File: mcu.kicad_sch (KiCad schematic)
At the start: 2 parts

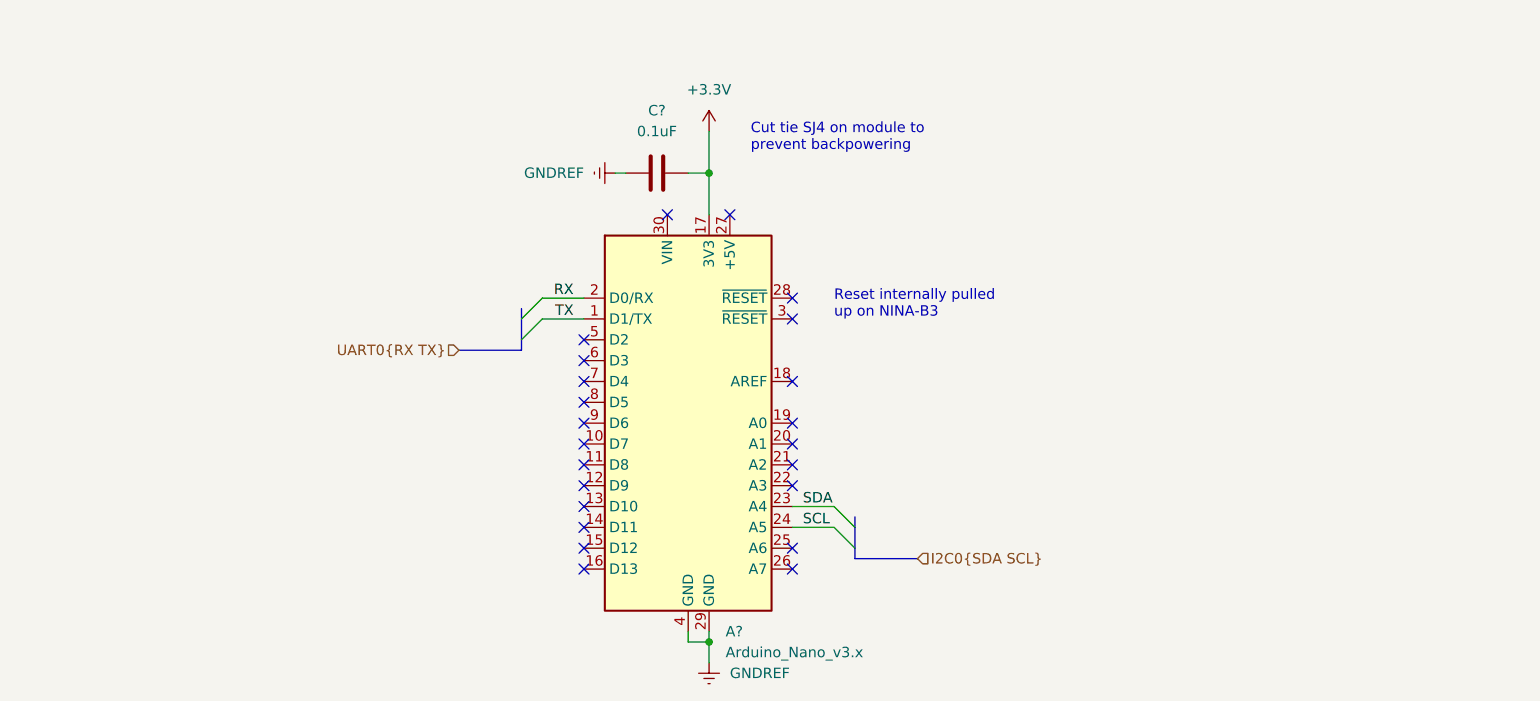
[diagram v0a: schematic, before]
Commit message: create IO busses
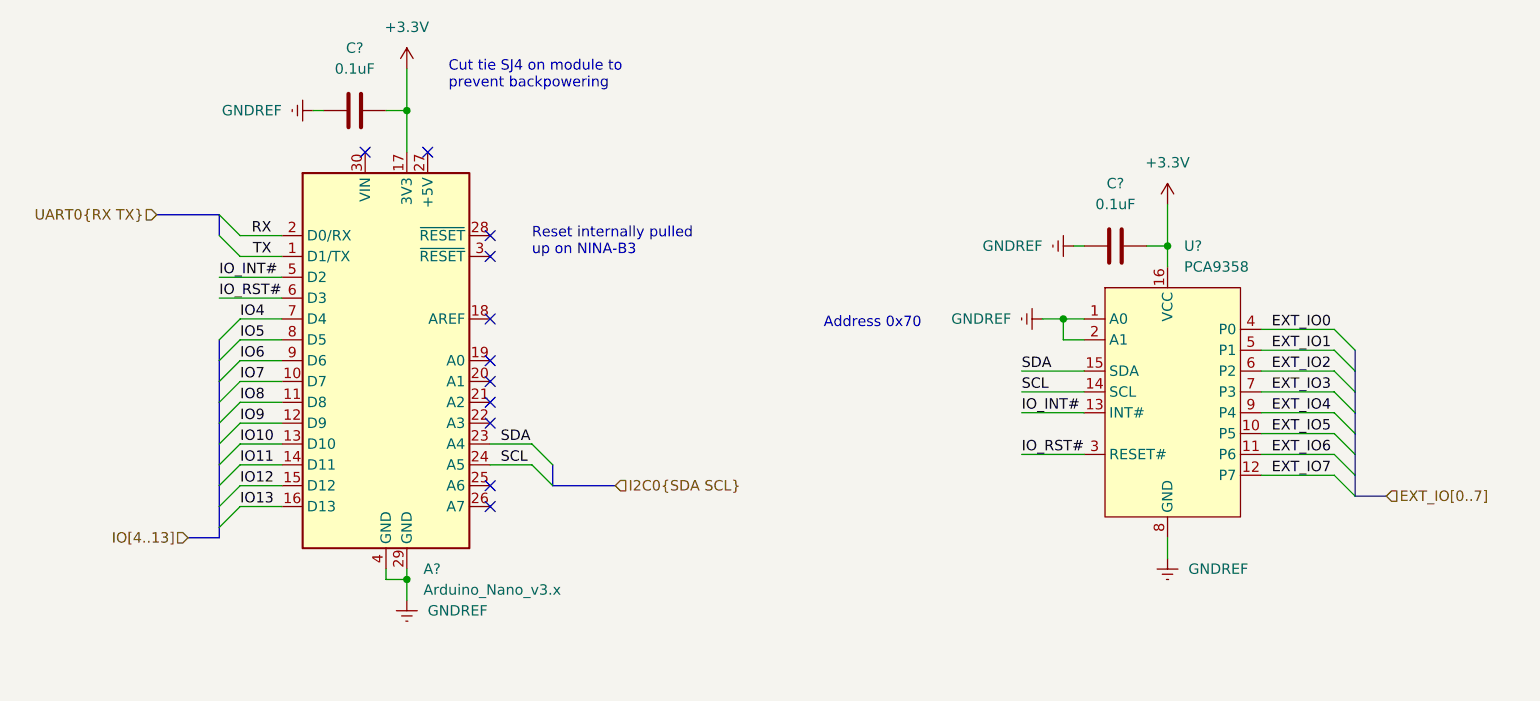
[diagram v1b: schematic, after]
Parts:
- added C?: 0.1uF, Capacitor_SMD:C_0805_2012Metric_Pad1.18x1.45mm_HandSolder, symbol Device:C
- added U?: PCA9358, Package_SO:SOIC-16W_7.5x10.3mm_P1.27mm, symbol Toadly:PCA9358
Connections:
- net +3.3V: now also C?.1, U?.16 (VCC)
- net GNDREF: now also C?.2, U?.1 (A0), U?.2 (A1), U?.8 (GND)
- net SCL: now also U?.14 (SCL)
- net SDA: now also U?.15 (SDA)
- net IO7: now reaches A?.10 (D7)
- net IO8: now reaches A?.11 (D8)
- net IO9: now reaches A?.12 (D9)
- net IO10: now reaches A?.13 (D10)
- net IO11: now reaches A?.14 (D11)
- net IO12: now reaches A?.15 (D12)
- net IO13: now reaches A?.16 (D13)
- net IO_INT#: now reaches A?.5 (D2)
- net IO_INT#: now also U?.13 (INT#)
- net IO_RST#: now reaches A?.6 (D3)
- net IO_RST#: now also U?.3 (RESET#)
- net IO4: now reaches A?.7 (D4)
- net IO5: now reaches A?.8 (D5)
- net IO6: now reaches A?.9 (D6)
- new net EXT_IO0: U?.4 (P0)
- new net EXT_IO1: U?.5 (P1)
- new net EXT_IO2: U?.6 (P2)
- new net EXT_IO3: U?.7 (P3)
- new net EXT_IO4: U?.9 (P4)
- new net EXT_IO5: U?.10 (P5)
- new net EXT_IO6: U?.11 (P6)
- new net EXT_IO7: U?.12 (P7)
- no-connect marks 23 -> 11
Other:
- note added: "Address 0x70"
- moved on the sheet: A?, C?

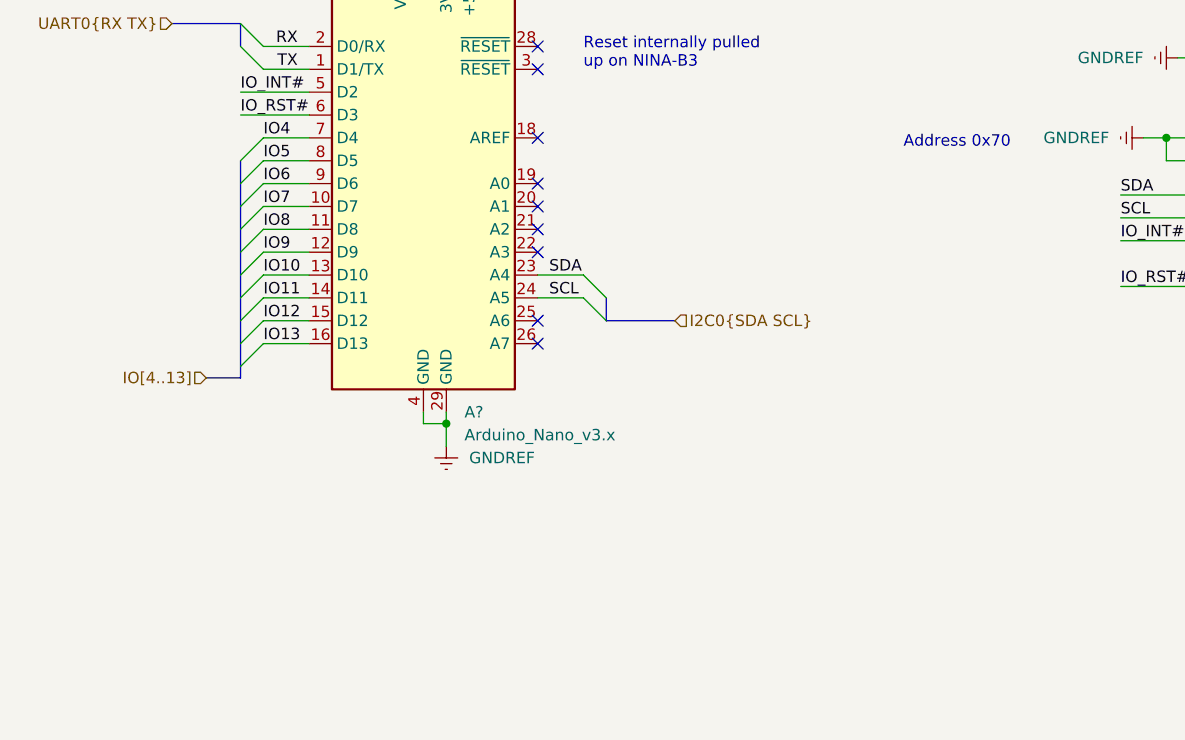
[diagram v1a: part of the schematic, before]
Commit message: add analog pins to IO and I2C pullup slots
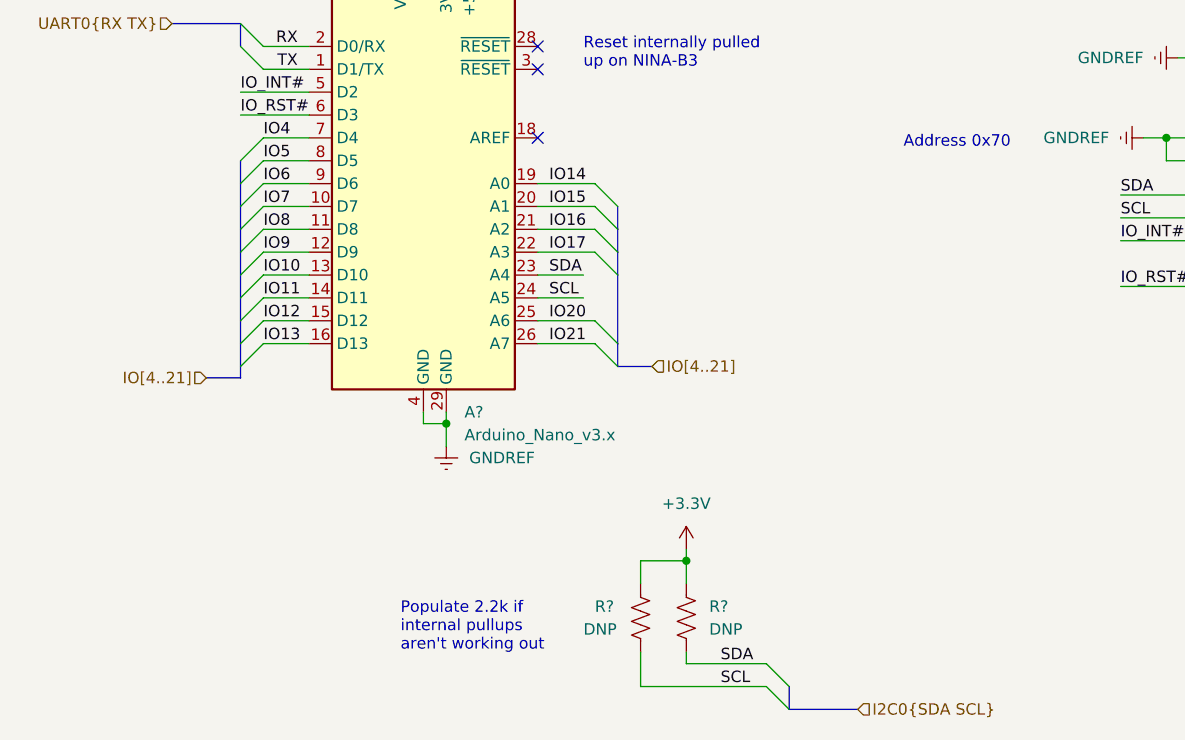
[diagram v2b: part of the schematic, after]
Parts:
- added R? (x2): DNP, Resistor_SMD:R_0805_2012Metric_Pad1.20x1.40mm_HandSolder, symbol Device:R_US
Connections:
- net +3.3V: now also R?.1, R?.2
- net SCL: now also R?.1
- net SDA: now also R?.2
- net IO14: now reaches A?.19 (A0)
- net IO15: now reaches A?.20 (A1)
- net IO16: now reaches A?.21 (A2)
- net IO17: now reaches A?.22 (A3)
- net IO20: now reaches A?.25 (A6)
- net IO21: now reaches A?.26 (A7)
- no-connect marks 11 -> 5
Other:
- note added: "Populate 2.2k if internal pullups aren't working out"

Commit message: annotate schematic
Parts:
- gave numbers to parts that had none: 6
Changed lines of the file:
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@@
   (symbol (lib_id "Device:C") (at 191.77 66.04 270) (mirror x) (unit 1)
     (in_bom yes) (on_board yes) (fields_autoplaced)
-    (property "Reference" "C?" (id 0) (at 191.77 58.42 90))
+    (property "Reference" "C6" (id 0) (at 191.77 58.42 90))
     (property "Value" "0.1uF" (id 1) (at 191.77 60.96 90))
     (property "Footprint" "Capacitor_SMD:C_0805_2012Metric_Pad1.18x1.45mm_HandSolder" (id 2) (at 187.96 65.0748 0)
@@
   (symbol (lib_id "Device:C") (at 99.06 49.53 270) (mirror x) (unit 1)
     (in_bom yes) (on_board yes) (fields_autoplaced)
-    (property "Reference" "C?" (id 0) (at 99.06 41.91 90))
+    (property "Reference" "C5" (id 0) (at 99.06 41.91 90))
     (property "Value" "0.1uF" (id 1) (at 99.06 44.45 90))
     (property "Footprint" "Capacitor_SMD:C_0805_2012Metric_Pad1.18x1.45mm_HandSolder" (id 2) (at 95.25 48.5648 0)
@@
   (symbol (lib_id "power:GNDREF") (at 93.98 49.53 270) (mirror x) (unit 1)
     (in_bom yes) (on_board yes) (fields_autoplaced)
-    (property "Reference" "#PWR?" (id 0) (at 87.63 49.53 0)
+    (property "Reference" "#PWR017" (id 0) (at 87.63 49.53 0)
       (effects (font (size 1.27 1.27)) hide)
     )
@@
   (symbol (lib_id "power:GNDREF") (at 186.69 66.04 270) (mirror x) (unit 1)
     (in_bom yes) (on_board yes) (fields_autoplaced)
-    (property "Reference" "#PWR?" (id 0) (at 180.34 66.04 0)
+    (property "Reference" "#PWR022" (id 0) (at 180.34 66.04 0)
       (effects (font (size 1.27 1.27)) hide)
     )
@@
   (symbol (lib_id "power:GNDREF") (at 182.88 74.93 270) (mirror x) (unit 1)
     (in_bom yes) (on_board yes) (fields_autoplaced)
-    (property "Reference" "#PWR?" (id 0) (at 176.53 74.93 0)
+    (property "Reference" "#PWR021" (id 0) (at 176.53 74.93 0)
       (effects (font (size 1.27 1.27)) hide)
     )
@@
   (symbol (lib_id "MCU_Module:Arduino_Nano_v3.x") (at 102.87 80.01 0) (unit 1)
     (in_bom yes) (on_board yes) (fields_autoplaced)
-    (property "Reference" "A?" (id 0) (at 107.4294 105.41 0)
+    (property "Reference" "A1" (id 0) (at 107.4294 105.41 0)
       (effects (font (size 1.27 1.27)) (justify left))
     )
@@
   (symbol (lib_id "power:+3.3V") (at 198.12 60.96 0) (unit 1)
     (in_bom yes) (on_board yes) (fields_autoplaced)
-    (property "Reference" "#PWR?" (id 0) (at 198.12 64.77 0)
+    (property "Reference" "#PWR023" (id 0) (at 198.12 64.77 0)
       (effects (font (size 1.27 1.27)) hide)
     )
@@
   (symbol (lib_id "power:+3.3V") (at 105.41 44.45 0) (unit 1)
     (in_bom yes) (on_board yes) (fields_autoplaced)
-    (property "Reference" "#PWR?" (id 0) (at 105.41 48.26 0)
+    (property "Reference" "#PWR018" (id 0) (at 105.41 48.26 0)
       (effects (font (size 1.27 1.27)) hide)
     )
@@
   (symbol (lib_id "power:+3.3V") (at 132.08 120.65 0) (unit 1)
     (in_bom yes) (on_board yes) (fields_autoplaced)
-    (property "Reference" "#PWR?" (id 0) (at 132.08 124.46 0)
+    (property "Reference" "#PWR020" (id 0) (at 132.08 124.46 0)
       (effects (font (size 1.27 1.27)) hide)
     )
@@
   (symbol (lib_id "Device:R_US") (at 127 128.27 180) (unit 1)
     (in_bom yes) (on_board yes)
-    (property "Reference" "R?" (id 0) (at 121.92 127 0)
+    (property "Reference" "R1" (id 0) (at 121.92 127 0)
       (effects (font (size 1.27 1.27)) (justify right))
     )
@@
   (symbol (lib_id "Device:R_US") (at 132.08 128.27 0) (unit 1)
     (in_bom yes) (on_board yes) (fields_autoplaced)
-    (property "Reference" "R?" (id 0) (at 134.62 126.9999 0)
+    (property "Reference" "R2" (id 0) (at 134.62 126.9999 0)
       (effects (font (size 1.27 1.27)) (justify left))
     )
@@
   (symbol (lib_id "power:GNDREF") (at 105.41 109.22 0) (unit 1)
     (in_bom yes) (on_board yes) (fields_autoplaced)
-    (property "Reference" "#PWR?" (id 0) (at 105.41 115.57 0)
+    (property "Reference" "#PWR019" (id 0) (at 105.41 115.57 0)
       (effects (font (size 1.27 1.27)) hide)
     )
@@
   (symbol (lib_id "Toadly:PCA9358") (at 198.12 85.09 0) (unit 1)
     (in_bom yes) (on_board yes) (fields_autoplaced)
-    (property "Reference" "U?" (id 0) (at 200.1394 66.04 0)
+    (property "Reference" "U3" (id 0) (at 200.1394 66.04 0)
       (effects (font (size 1.27 1.27)) (justify left))
     )
@@
   (symbol (lib_id "power:GNDREF") (at 198.12 104.14 0) (unit 1)
     (in_bom yes) (on_board yes) (fields_autoplaced)
-    (property "Reference" "#PWR?" (id 0) (at 198.12 110.49 0)
-      (effects (font (size 1.27 1.27)) hide)
-    )
+    (property "Reference" "#PWR024" (id 0) (at 198.12 110.49 0)
+      (effects (font (size 1.27 1.27)) hide)
+    )

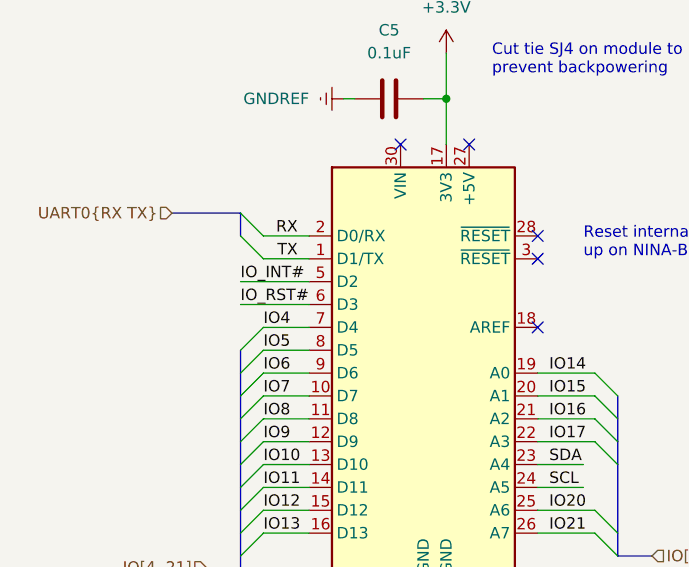
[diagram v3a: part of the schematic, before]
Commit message: many changes, update to KiCAD 7
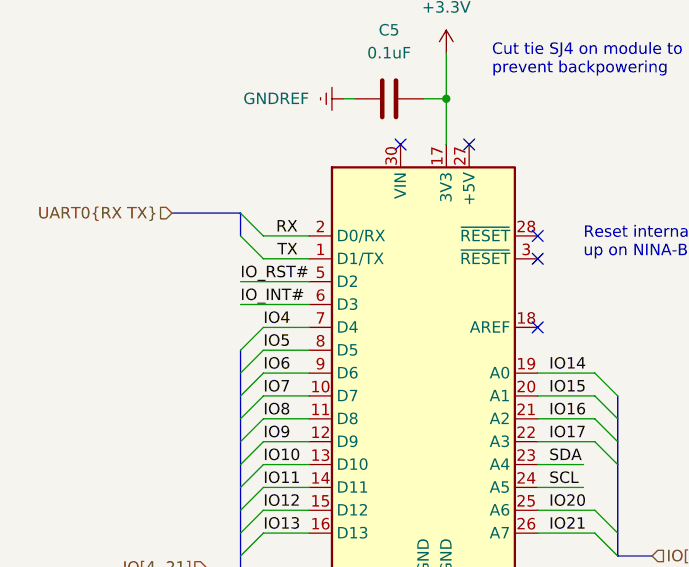
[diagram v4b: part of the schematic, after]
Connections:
- net IO_INT#: now also A1.6 (D3); no longer A1.5 (D2)
- net IO_RST#: now also A1.5 (D2); no longer A1.6 (D3)
